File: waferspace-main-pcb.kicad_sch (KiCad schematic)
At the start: 88 parts, among them J1 Conn_01x03, J12 Conn_01x03, J13 613012243121, J14 Conn_01x03, J17 Conn_01x03, J2 Conn_01x03, J20 USB_C, J3 613012243121, J4 Conn_02x35_Counter_Clockwise, J5 613012243121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

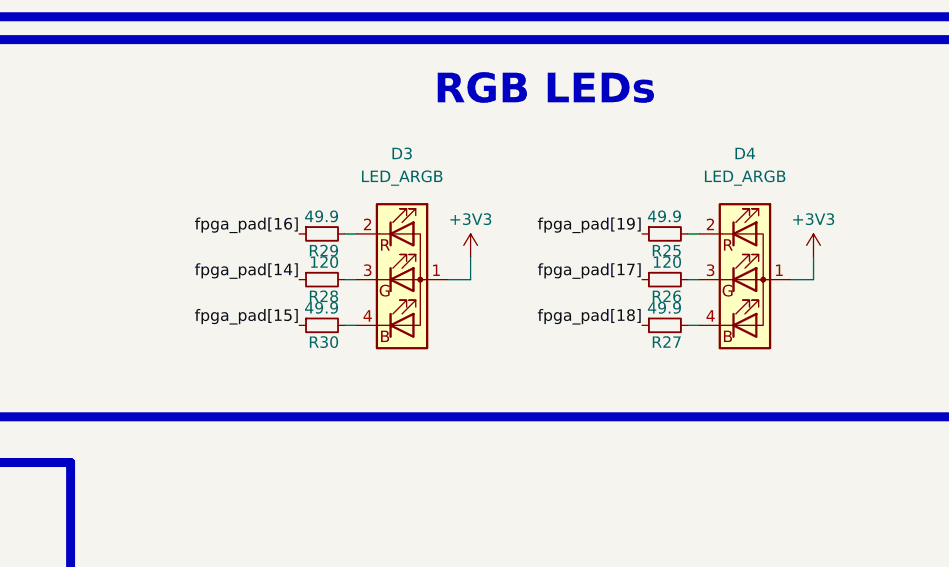
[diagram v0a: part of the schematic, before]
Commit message: Fix RGB LEDs
Signed-off-by: Leo Moser <leomoser99@gmail.com>
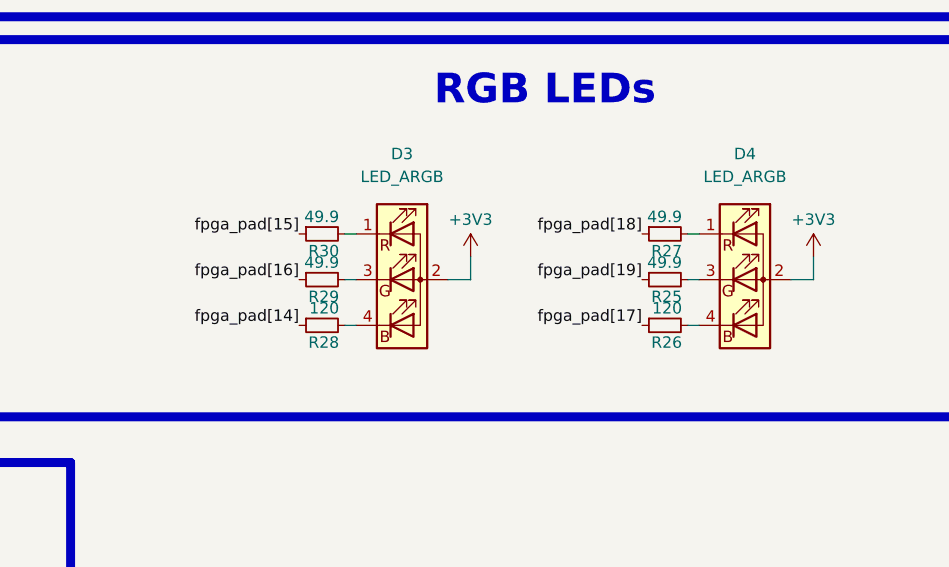
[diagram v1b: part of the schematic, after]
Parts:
- D3, D4: symbol Device:LED_ARGB -> Device:LED_RAGB
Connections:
- net +3V3: now also D3.2 (A), D4.2 (A); no longer D3.1 (A), D4.1 (A)
- net at R30.2: now also D3.1 (RK); no longer D3.4 (BK)
- net at R29.2: now also D3.3 (GK); no longer D3.2 (RK)
- net at R25.2: now also D4.3 (GK); no longer D4.2 (RK)
- net at R26.2: now also D4.4 (BK); no longer D4.3 (GK)
- net at R27.2: now also D4.1 (RK); no longer D4.4 (BK)
- net at R28.2: now also D3.4 (BK); no longer D3.3 (GK)
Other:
- moved on the sheet: R25, R26, R27, R28, R29, R30
